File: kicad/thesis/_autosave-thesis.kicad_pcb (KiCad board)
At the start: 2 copper layers, 85 x 60 mm, 14 parts, among them Q1 IRLZB8721, SW1 SW_DIP_x01, U1 INA219AxD

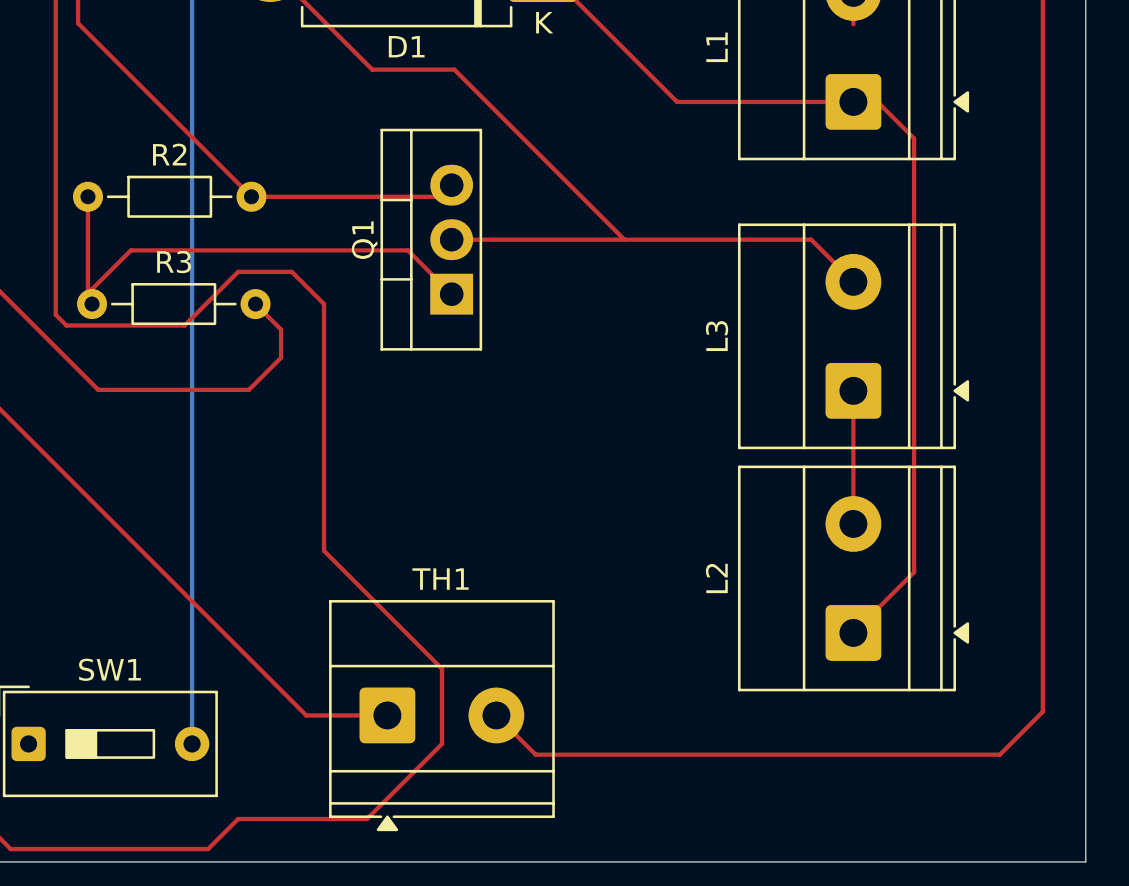
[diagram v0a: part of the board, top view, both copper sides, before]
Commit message: Roy suggestion part 2
Added pin sockets and terminal blocks for the load cell, INA219, and thermistor
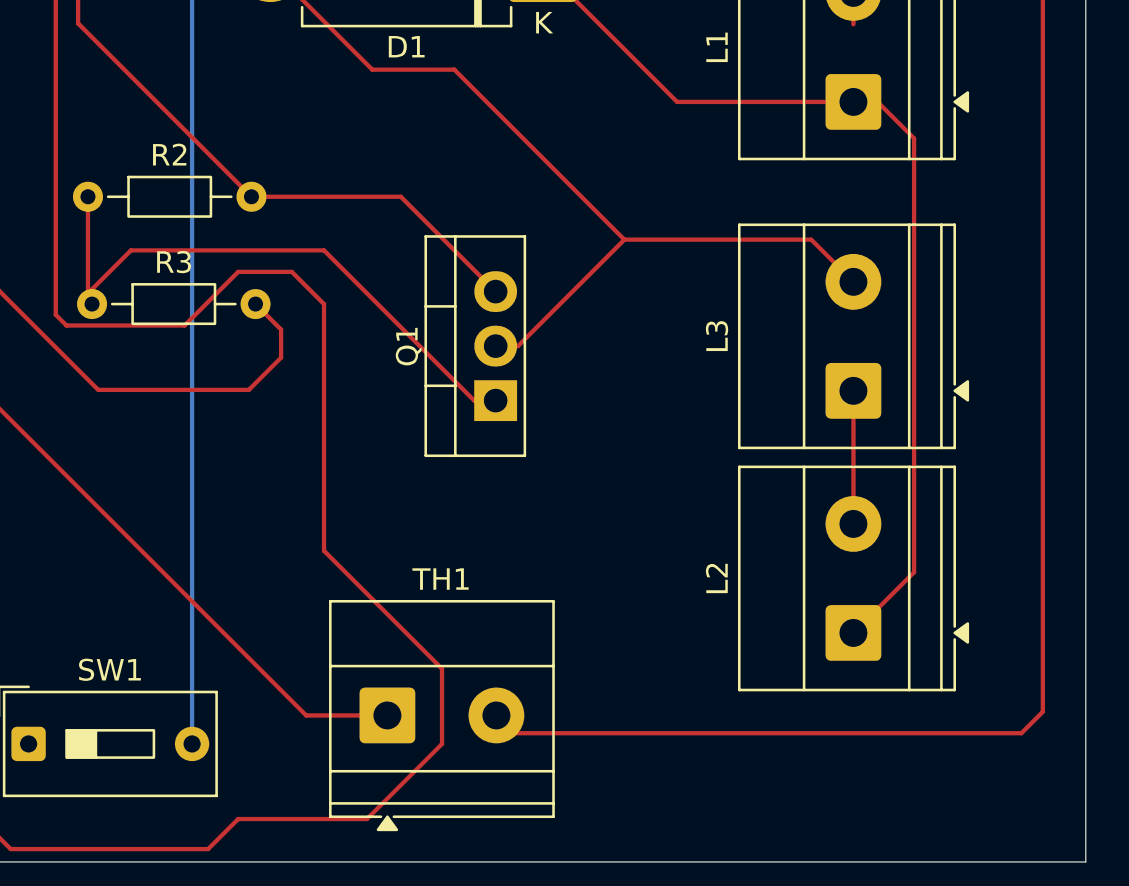
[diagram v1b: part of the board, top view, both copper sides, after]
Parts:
- moved Q1 5.37 mm to (111.5, 108.5)
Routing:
- net Net-(Q1-G): track 24.7 -> 28.8 mm
- net GND: track 202.6 -> 206.2 mm
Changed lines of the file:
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@@
 	(footprint "Package_TO_SOT_THT:TO-220-3_Vertical"
 		(layer "F.Cu")
-		(at 109.45 103.54 90)
+		(at 111.5 108.5 90)
 		(descr "TO-220-3, Vertical, RM 2.54mm, see https://www.vishay.com/docs/66542/to-220-1.pdf")
 		(tags "TO-220-3 Vertical RM 2.54mm")
@@
 	)
 	(segment
-		(start 84 73)
-		(end 90.5 73)
+		(start 111.5 103.42)
+		(end 107.08 99)
 		(width 0.2)
 		(layer "F.Cu")
@@
 	)
 	(segment
-		(start 113.3625 125)
-		(end 135 125)
+		(start 84 73)
+		(end 90.5 73)
 		(width 0.2)
 		(layer "F.Cu")
@@
 	)
 	(segment
-		(start 135 125)
-		(end 137 123)
-		(width 0.2)
-		(layer "F.Cu")
-		(net "GND")
-	)
-	(segment
-		(start 108.91 99)
-		(end 109.45 98.46)
+		(start 137 73)
+		(end 135 71)
 		(width 0.2)
 		(layer "F.Cu")
@@
 	)
 	(segment
-		(start 111.535 123.1725)
-		(end 113.3625 125)
+		(start 110.96 103.96)
+		(end 111.5 103.42)
 		(width 0.2)
 		(layer "F.Cu")
@@
 	)
 	(segment
-		(start 137 73)
-		(end 135 71)
+		(start 82.5 74.5)
+		(end 84 73)
 		(width 0.2)
 		(layer "F.Cu")
@@
 	)
 	(segment
-		(start 82.5 74.5)
-		(end 84 73)
+		(start 112.3625 124)
+		(end 136 124)
 		(width 0.2)
 		(layer "F.Cu")
@@
 	)
 	(segment
-		(start 96.54 71)
-		(end 92.04 75.5)
+		(start 136 124)
+		(end 137 123)
 		(width 0.2)
 		(layer "F.Cu")
@@
 	)
 	(segment
-		(start 100.12 99)
-		(end 108.91 99)
+		(start 137 123)
+		(end 137 73)
 		(width 0.2)
 		(layer "F.Cu")
@@
 	)
 	(segment
-		(start 137 123)
-		(end 137 73)
+		(start 67.802 84.198)
+		(end 77.62 84.198)
 		(width 0.2)
 		(layer "F.Cu")
@@
 	)
 	(segment
-		(start 67.802 84.198)
-		(end 77.62 84.198)
+		(start 111.535 123.1725)
+		(end 112.3625 124)
 		(width 0.2)
 		(layer "F.Cu")
@@
 	)
 	(segment
+		(start 96.54 71)
+		(end 92.04 75.5)
+		(width 0.2)
+		(layer "F.Cu")
+		(net "GND")
+	)
+	(segment
+		(start 107.08 99)
+		(end 100.12 99)
+		(width 0.2)
+		(layer "F.Cu")
+		(net "GND")
+	)
+	(segment
 		(start 100.12 99)
 		(end 92.04 90.92)
@@
 	)
 	(segment
+		(start 110.5 108.5)
+		(end 103.5 101.5)
+		(width 0.2)
+		(layer "F.Cu")
+		(net "Net-(Q1-G)")
+	)
+	(segment
 		(start 92.5 103.81)
 		(end 92.69 104)
@@
 	(segment
 		(start 94.5 101.5)
-		(end 107.41 101.5)
+		(end 103.5 101.5)
 		(width 0.2)
 		(layer "F.Cu")
@@
 	)
 	(segment
-		(start 107.41 101.5)
-		(end 109.45 103.54)
+		(start 92.69 104)
+		(end 92.69 103.81)
 		(width 0.2)
 		(layer "F.Cu")
@@
 	)
 	(segment
-		(start 92.69 104)
-		(end 92.69 103.81)
+		(start 111.5 108.5)
+		(end 110.5 108.5)
 		(width 0.2)
 		(layer "F.Cu")
@@
 	)
 	(segment
-		(start 109.45 101)
-		(end 117.5 101)
-		(width 0.2)
-		(layer "F.Cu")
-		(net "Net-(D1-A)")
-	)
-	(segment
 		(start 101 77.575)
 		(end 101 74.425)
@@
 		(end 117.5 101)
 		(width 0.2)
+		(layer "F.Cu")
+		(net "Net-(D1-A)")
+	)
+	(segment
+		(start 111.5 105.96)
+		(end 112.54 105.96)
+		(width 0.2)
+		(layer "F.Cu")
+		(net "Net-(D1-A)")
+	)
+	(segment
+		(start 112.54 105.96)
+		(end 117.5 101)
+		(width 0.2)
